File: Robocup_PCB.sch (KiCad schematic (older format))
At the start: 39 parts

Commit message: Finished schematic, started PCB Design
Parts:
- added D1: 1N5347B, Diode_THT:D_DO-201_P15.24mm_Horizontal, symbol Diode:1N53xxB
- added D2: GREEN, LED_SMD:LED_0805_2012Metric_Pad1.15x1.40mm_HandSolder, symbol Device:LED
- added J1: M1_ENOUT, Connector_PinSocket_2.54mm:PinSocket_1x02_P2.54mm_Vertical, symbol Connector:Conn_01x02_Male
- added J3: M2_ENOUT, Connector_PinSocket_2.54mm:PinSocket_1x02_P2.54mm_Vertical, symbol Connector:Conn_01x02_Male
- added J5: M3_ENOUT, Connector_PinSocket_2.54mm:PinSocket_1x02_P2.54mm_Vertical, symbol Connector:Conn_01x02_Male
- added J7: Arduino_Mega_Header, w_conn_misc:arduino_mega_header, symbol w_connectors:Arduino_Mega_Header
- added J8: XT60-M, 3rd party libs:AMASS_XT60-M, symbol XT60-M:XT60-M
- added Q1: IRF9540N, Package_TO_SOT_THT:TO-220-3_Vertical, symbol Transistor_FET:IRF9540N
- added Q2: IRFR120ZTRPBF, 3rd party libs:DPAK229P990X239-3N, symbol IRFR120ZTRPBF:IRFR120ZTRPBF
- added R13: 100k, Resistor_SMD:R_1206_3216Metric_Pad1.42x1.75mm_HandSolder, symbol Device:R
- added R14: 140R, Resistor_SMD:R_1206_3216Metric_Pad1.42x1.75mm_HandSolder, symbol Device:R
- added SW1: SS ESP101, Connector_PinSocket_2.54mm:PinSocket_1x03_P2.54mm_Vertical, symbol Switch:SW_SPDT
- added U1, U2: TB6612FNG_MOD, Robocup_PCB:U_TB6612FNG_MOD, symbol Robocup_PCB:TB6612FNG_MOD
- added U3: 5V_D24V5F5, Robocup_PCB:5V_D24V5F5_FP, symbol Robocup_PCB:5V_D24V5F5
- added U4: 12V_S18V20F12, Robocup_PCB:12_S18V20F12_FP, symbol Robocup_PCB:12V_S18V20F12
- C1, C10, C11, C12, C2, C3, C4, C5, C6, C7, C8, C9: value 1uF -> 0.1uF
- J2, J4, J6: renamed from J?; footprint (none) -> Connector_PinSocket_2.54mm:PinSocket_1x06_P2.54mm_Vertical
- R1, R10, R11, R12, R2, R3, R4, R5, R6, R7, R8, R9: value 62K -> 6k2
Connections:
- net labels added: +12V, +5V, M1_A, M1_AIN1, M1_AIN2, M1_B, M1_PWMA, M2_A, M2_B, M2_BIN1, M2_BIN2, M2_PWMB, M3_A, M3_AIN1, M3_AIN2, M3_B, M3_PWMA
- wire segments 72 -> 178
- no-connect marks 0 -> 69
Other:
- moved on the sheet: J2, J4, J6

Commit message: Redid power management, more efficient
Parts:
- removed Q2: IRFR120ZTRPBF, 3rd party libs:DPAK229P990X239-3N, symbol IRFR120ZTRPBF:IRFR120ZTRPBF
- added C?: 10n, symbol Device:C
- added D?: RED, LED_SMD:LED_0805_2012Metric_Pad1.15x1.40mm_HandSolder, symbol Device:LED
- added D?: BLUE, LED_SMD:LED_0805_2012Metric_Pad1.15x1.40mm_HandSolder, symbol Device:LED
- added R?: 680R, Resistor_SMD:R_1206_3216Metric_Pad1.42x1.75mm_HandSolder, symbol Device:R
- added R?: 180R, Resistor_SMD:R_1206_3216Metric_Pad1.42x1.75mm_HandSolder, symbol Device:R
- added SW? (x2): SS ESP101, Connector_PinSocket_2.54mm:PinSocket_1x03_P2.54mm_Vertical, symbol Switch:SW_SPDT
- R14: value 140R -> 680R
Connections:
- wire segments 178 -> 195
- no-connect marks 69 -> 70
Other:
- moved on the sheet: D1, D2, J8, Q1, R13, R14, SW1, U3, U4

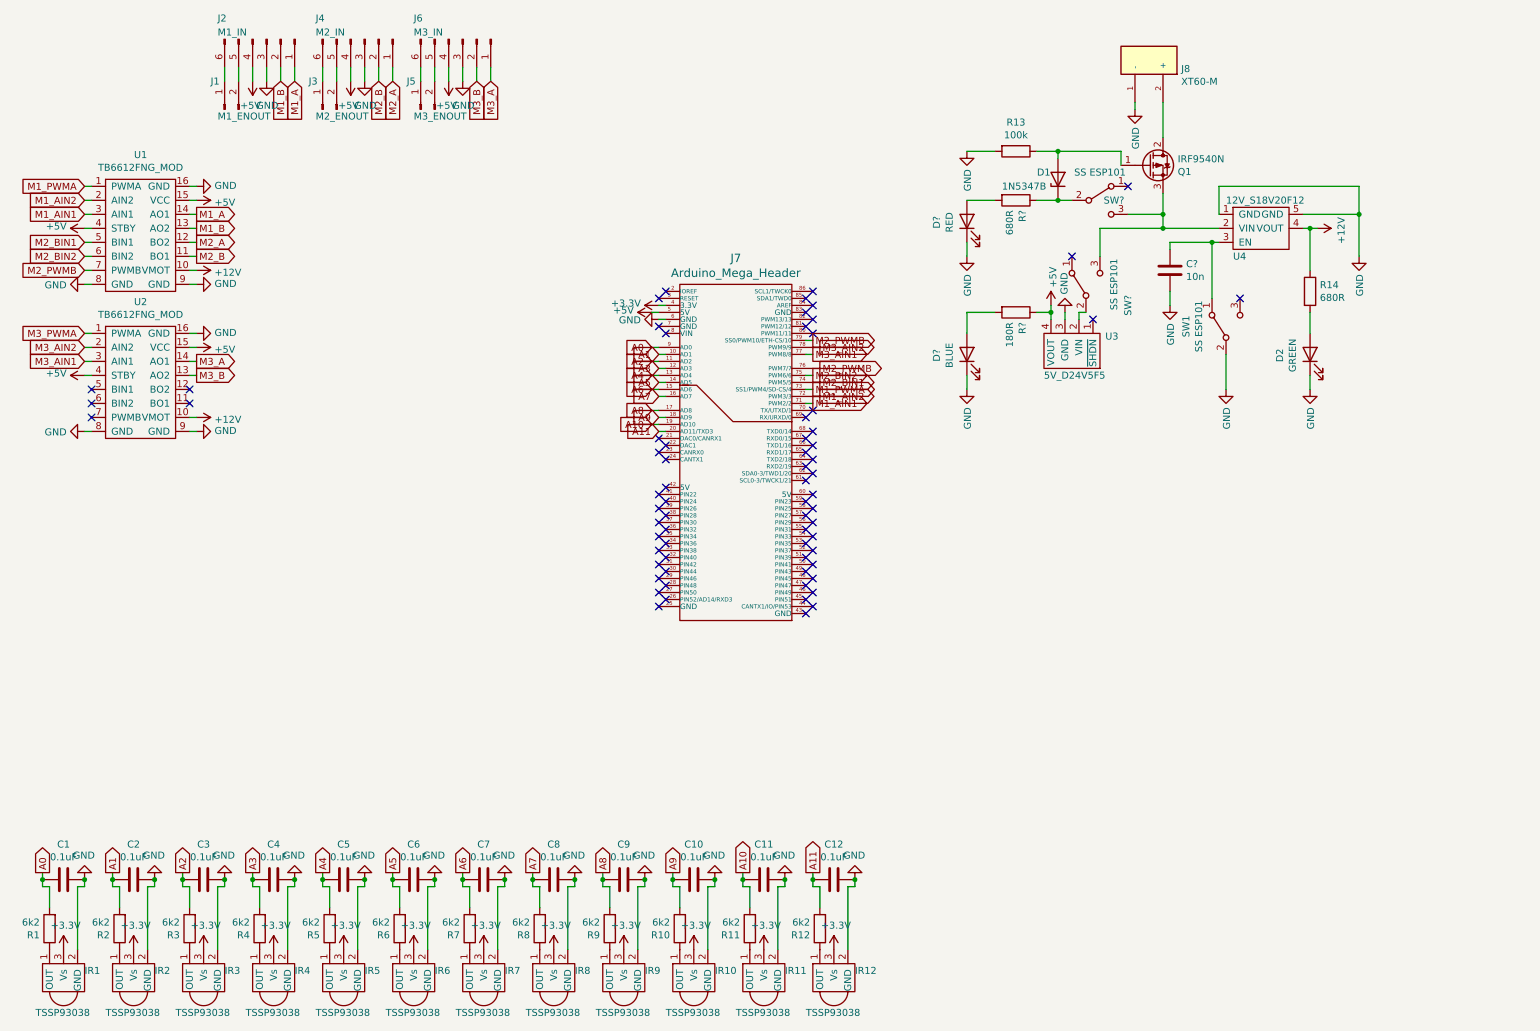
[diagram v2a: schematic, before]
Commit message: Parts given Footprints
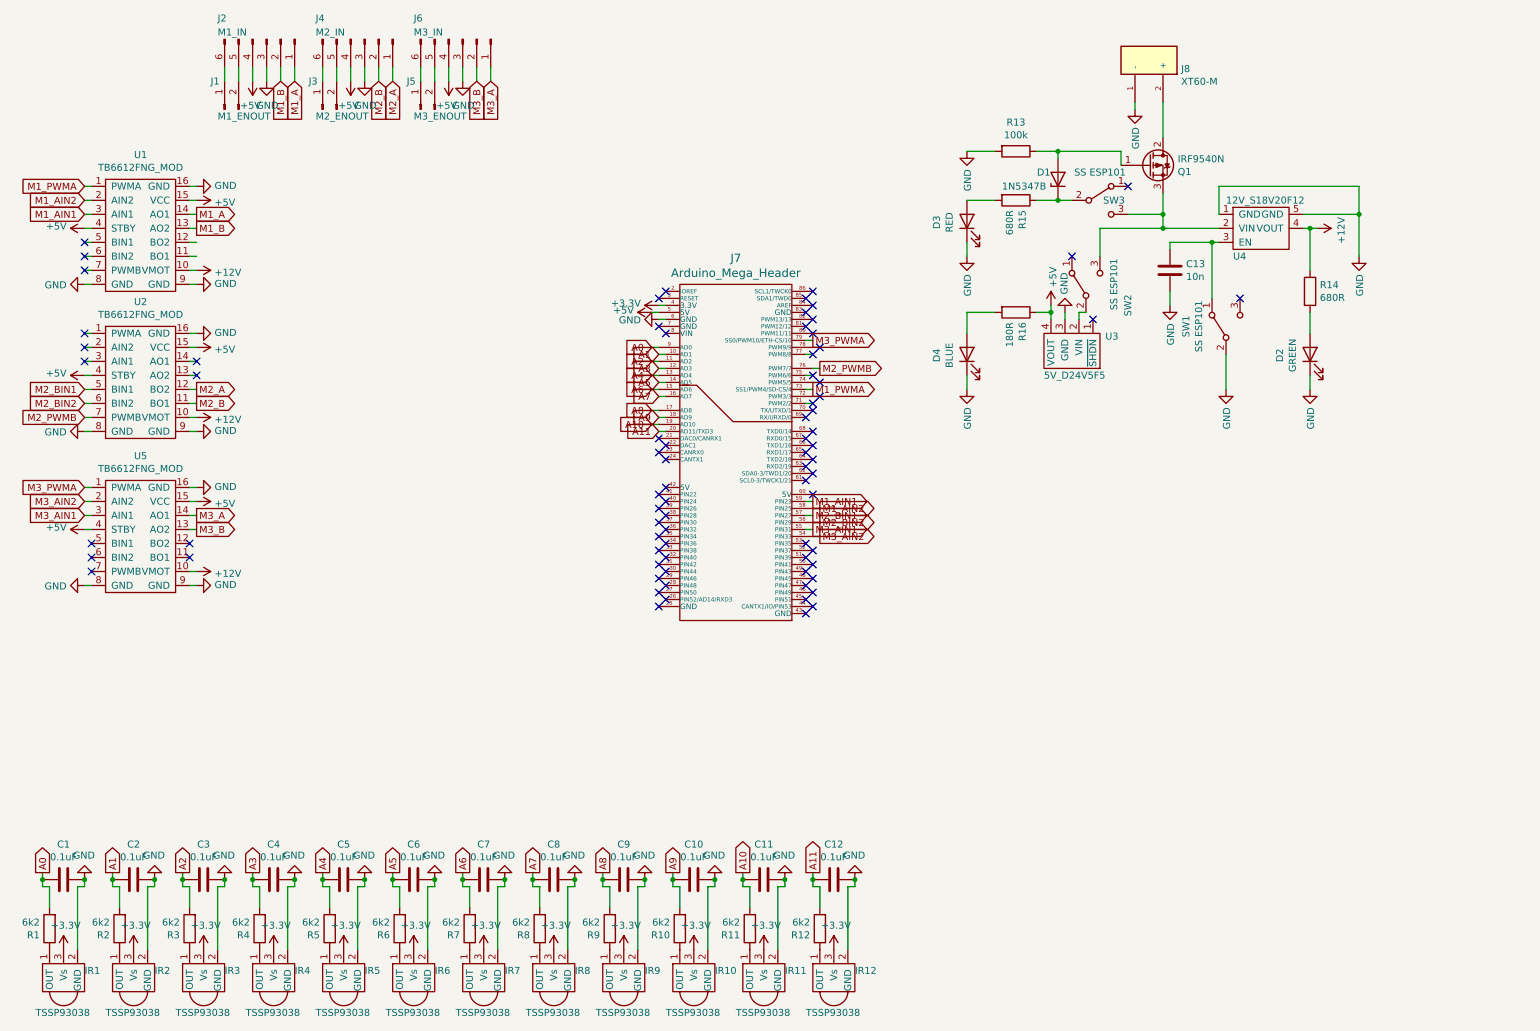
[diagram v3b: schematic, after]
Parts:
- added U2: TB6612FNG_MOD, Robocup_PCB:U_TB6612FNG_MOD, symbol Robocup_PCB:TB6612FNG_MOD
- C13: renamed from C?; footprint (none) -> Capacitor_SMD:C_0603_1608Metric_Pad1.05x0.95mm_HandSolder
- R13: footprint Resistor_SMD:R_1206_3216Metric_Pad1.42x1.75mm_HandSolder -> Resistor_SMD:R_0805_2012Metric_Pad1.15x1.40mm_HandSolder
- gave numbers to parts that had none: 6
- renumbered U2 to U5
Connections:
- net +12V: now also U2.10 (VMOT)
- net +5V: now also U2.15 (VCC), U2.4 (STBY)
- net GND: now also U2.16 (GND), U2.8 (GND), U2.9 (GND)
- net M1_AIN1: now also J7.59 (PIN23); no longer J7.71 (PWM2/2)
- net M1_AIN2: now also J7.58 (PIN25); no longer J7.72 (PWM3/3)
- net M2_A: now also U2.12 (BO2); no longer U1.12 (BO2)
- net M2_B: now also U2.11 (BO1); no longer U1.11 (BO1)
- net M2_BIN1: now also J7.57 (PIN27), U2.5 (BIN1); no longer J7.74 (PWM5/5), U1.5 (BIN1)
- net M2_BIN2: now also J7.56 (PIN29), U2.6 (BIN2); no longer J7.75 (PWM6/6), U1.6 (BIN2)
- net M2_PWMB: now also U2.7 (PWMB); no longer J7.79 (SS0/PWM10/ETH-CS/10), U1.7 (PWMB)
- net M3_AIN1: now also J7.55 (PIN31); no longer J7.77 (PWM8/8)
- net M3_AIN2: now also J7.54 (PIN33); no longer J7.78 (PWM9/9)
- net M3_PWMA: now also J7.79 (SS0/PWM10/ETH-CS/10)
- no-connect marks 70 -> 78
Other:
- moved on the sheet: U5

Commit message: Finished PCB, Generated Gerbers
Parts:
- removed J1: M1_ENOUT, Connector_PinSocket_2.54mm:PinSocket_1x02_P2.54mm_Vertical, symbol Connector:Conn_01x02_Male
- removed J3: M2_ENOUT, Connector_PinSocket_2.54mm:PinSocket_1x02_P2.54mm_Vertical, symbol Connector:Conn_01x02_Male
- removed J5: M3_ENOUT, Connector_PinSocket_2.54mm:PinSocket_1x02_P2.54mm_Vertical, symbol Connector:Conn_01x02_Male
- C13: footprint Capacitor_SMD:C_0603_1608Metric_Pad1.05x0.95mm_HandSolder -> Capacitor_SMD:C_1206_3216Metric_Pad1.42x1.75mm_HandSolder
- Q1: footprint Package_TO_SOT_THT:TO-220-3_Vertical -> Package_TO_SOT_SMD:TO-263-2
- R13: footprint Resistor_SMD:R_0805_2012Metric_Pad1.15x1.40mm_HandSolder -> Resistor_SMD:R_1206_3216Metric_Pad1.42x1.75mm_HandSolder
- U3: footprint Robocup_PCB:5V_D24V5F5_FP -> (none)
- renumbered J2 to J1, J4 to J2, J6 to J3, J7 to J4
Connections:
- net M3_ENB: now reaches J4.39 (PIN26)
- net M3_ENB: now also J3.6 (Pin_6)
- net M2_ENB: now reaches J4.40 (PIN24)
- net M2_ENB: now also J2.6 (Pin_6)
- net M1_ENB: now reaches J4.41 (PIN22)
- net M1_ENB: now also J1.6 (Pin_6)
- net M3_ENA: now reaches J4.62 (SDA0-3/TWD1/20)
- net M3_ENA: now also J3.5 (Pin_5)
- net M2_ENA: now reaches J4.63 (RXD2/19)
- net M2_ENA: now also J2.5 (Pin_5)
- net M1_ENA: now reaches J4.64 (TXD2/18)
- net M1_ENA: now also J1.5 (Pin_5)
- no-connect marks 78 -> 72
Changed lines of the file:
@@
 A11
 $Comp
-L Connector:Conn_01x06_Male J2
+L Connector:Conn_01x06_Male J1
 U 1 1 5FFBF4FE
 P 2250 750
-F 0 "J2" V 2100 400 50  0000 L CNN
+F 0 "J1" V 2100 400 50  0000 L CNN
 F 1 "M1_IN" V 2200 400 50  0000 L CNN
 F 2 "Connector_PinSocket_2.54mm:PinSocket_1x06_P2.54mm_Vertical" H 2250 750 50  0001 C CNN
@@
 $EndComp
 $Comp
-L Connector:Conn_01x06_Male J6
+L Connector:Conn_01x06_Male J3
 U 1 1 5FFC7622
 P 3650 750
-F 0 "J6" V 3500 400 50  0000 L CNN
+F 0 "J3" V 3500 400 50  0000 L CNN
 F 1 "M3_IN" V 3600 400 50  0000 L CNN
 F 2 "Connector_PinSocket_2.54mm:PinSocket_1x06_P2.54mm_Vertical" H 3650 750 50  0001 C CNN
@@
 $EndComp
 $Comp
-L Connector:Conn_01x06_Male J4
+L Connector:Conn_01x06_Male J2
 U 1 1 5FFC2FEB
 P 2950 750
-F 0 "J4" V 2800 400 50  0000 L CNN
+F 0 "J2" V 2800 400 50  0000 L CNN
 F 1 "M2_IN" V 2900 400 50  0000 L CNN
 F 2 "Connector_PinSocket_2.54mm:PinSocket_1x06_P2.54mm_Vertical" H 2950 750 50  0001 C CNN
@@
 $EndComp
 $Comp
-L w_connectors:Arduino_Mega_Header J7
+L w_connectors:Arduino_Mega_Header J4
 U 1 1 5FF3CCD5
 P 5600 3700
-F 0 "J7" H 5600 5087 60  0000 C CNN
+F 0 "J4" H 5600 5087 60  0000 C CNN
 F 1 "Arduino_Mega_Header" H 5600 4981 60  0000 C CNN
 F 2 "w_conn_misc:arduino_mega_header" H 5600 3700 60  0001 C CNN
@@
 Wire Wire Line
 	2150 950  2150 1050
-$Comp
-L Connector:Conn_01x02_Male J5
-U 1 1 6006A0CE
-P 3350 1250
-F 0 "J5" V 3550 1350 50  0000 R CNN
-F 1 "M3_ENOUT" V 3300 1300 50  0000 R CNN
-F 2 "Connector_PinSocket_2.54mm:PinSocket_1x02_P2.54mm_Vertical" H 3350 1250 50  0001 C CNN
-F 3 "~" H 3350 1250 50  0001 C CNN
-	1    3350 1250
-	0    -1   -1   0
-$EndComp
-$Comp
-L Connector:Conn_01x02_Male J3
-U 1 1 6006B547
-P 2650 1250
-F 0 "J3" V 2850 1350 50  0000 R CNN
-F 1 "M2_ENOUT" V 2600 1300 50  0000 R CNN
-F 2 "Connector_PinSocket_2.54mm:PinSocket_1x02_P2.54mm_Vertical" H 2650 1250 50  0001 C CNN
-F 3 "~" H 2650 1250 50  0001 C CNN
-	1    2650 1250
-	0    -1   -1   0
-$EndComp
-$Comp
-L Connector:Conn_01x02_Male J1
-U 1 1 6006BCDF
-P 1950 1250
-F 0 "J1" V 2150 1350 50  0000 R CNN
-F 1 "M1_ENOUT" V 1900 1300 50  0000 R CNN
-F 2 "Connector_PinSocket_2.54mm:PinSocket_1x02_P2.54mm_Vertical" H 1950 1250 50  0001 C CNN
-F 3 "~" H 1950 1250 50  0001 C CNN
-	1    1950 1250
-	0    -1   -1   0
-$EndComp
-Wire Wire Line
-	3450 950  3450 1050
-Wire Wire Line
-	3350 950  3350 1050
-Wire Wire Line
-	2750 950  2750 1050
-Wire Wire Line
-	2650 950  2650 1050
-Wire Wire Line
-	2050 950  2050 1050
-Wire Wire Line
-	1950 950  1950 1050
 Text GLabel 1750 2000 2    50   Output ~ 0
 M1_A
@@
 NoConn ~ 6150 3650
 NoConn ~ 6100 3700
-NoConn ~ 6150 3750
-NoConn ~ 6100 3800
-NoConn ~ 6150 3850
 NoConn ~ 6100 3900
 NoConn ~ 6150 4000
@@
 NoConn ~ 5050 4200
 NoConn ~ 5100 4150
-NoConn ~ 5050 4100
-NoConn ~ 5100 4050
-NoConn ~ 5050 4000
 NoConn ~ 5100 3950
 $Comp
@@
 F 0 "Q1" H 8755 1604 50  0000 L CNN
 F 1 "IRF9540N" H 8755 1695 50  0000 L CNN
-F 2 "Package_TO_SOT_THT:TO-220-3_Vertical" H 8750 1575 50  0001 L CIN
+F 2 "Package_TO_SOT_SMD:TO-263-2" H 8750 1575 50  0001 L CIN
 F 3 "http://www.irf.com/product-info/datasheets/data/irf9540n.pdf" H 8550 1650 50  0001 L CNN
 	1    8550 1650
@@
 F 0 "R13" V 7393 1550 50  0000 C CNN
 F 1 "100k" V 7484 1550 50  0000 C CNN
-F 2 "Resistor_SMD:R_0805_2012Metric_Pad1.15x1.40mm_HandSolder" V 7530 1550 50  0001 C CNN
+F 2 "Resistor_SMD:R_1206_3216Metric_Pad1.42x1.75mm_HandSolder" V 7530 1550 50  0001 C CNN
 F 3 "~" H 7600 1550 50  0001 C CNN
 	1    7600 1550
@@
 Wire Wire Line
 	9750 2100 9700 2100
-$Comp
-L Robocup_PCB:5V_D24V5F5 U3
-U 1 1 604D36B7
-P 8000 2950
-F 0 "U3" H 7762 2871 50  0000 R CNN
-F 1 "5V_D24V5F5" H 8200 3150 50  0000 R CNN
-F 2 "Robocup_PCB:5V_D24V5F5_FP" H 7950 2900 50  0001 C CNN
-F 3 "" H 7950 2900 50  0001 C CNN
-	1    8000 2950
-	-1   0    0    1
-$EndComp
 NoConn ~ 8150 2750
 $Comp
@@
 F 0 "C13" H 8815 2446 50  0000 L CNN
 F 1 "10n" H 8815 2355 50  0000 L CNN
-F 2 "Capacitor_SMD:C_0603_1608Metric_Pad1.05x0.95mm_HandSolder" H 8738 2250 50  0001 C CNN
+F 2 "Capacitor_SMD:C_1206_3216Metric_Pad1.42x1.75mm_HandSolder" H 8738 2250 50  0001 C CNN
 F 3 "~" H 8700 2400 50  0001 C CNN
 	1    8700 2400
@@
 	-1   0    0    1
 $EndComp
+Text GLabel 2050 1100 3    50   Output ~ 0
+M1_ENA
+Wire Wire Line
+	2050 950  2050 1100
+Text GLabel 6200 3750 2    50   Input ~ 0
+M1_ENA
+Wire Wire Line
+	6150 3750 6200 3750
+Text GLabel 2750 1100 3    50   Output ~ 0
+M2_ENA
+Wire Wire Line
+	2750 950  2750 1100
+Text GLabel 3450 1100 3    50   Output ~ 0
+M3_ENA
+Wire Wire Line
+	3450 950  3450 1100
+Text GLabel 6150 3800 2    50   Input ~ 0
+M2_ENA
+Wire Wire Line
+	6100 3800 6150 3800
+Text GLabel 6200 3850 2    50   Input ~ 0
+M3_ENA
+Wire Wire Line
+	6150 3850 6200 3850
+Text GLabel 1950 1100 3    50   Output ~ 0
+M1_ENB
+Wire Wire Line
+	1950 950  1950 1100
+Text GLabel 5000 4000 0    50   Input ~ 0
+M1_ENB
+Wire Wire Line
+	5000 4000 5050 4000
+Text GLabel 2650 1100 3    50   Output ~ 0
+M2_ENB
+Wire Wire Line
+	2650 950  2650 1100
+Text GLabel 3350 1100 3    50   Output ~ 0
+M3_ENB
+Wire Wire Line
+	3350 950  3350 1100
+Text GLabel 5050 4050 0    50   Input ~ 0
+M2_ENB
+Wire Wire Line
+	5050 4050 5100 4050
+Text GLabel 5000 4100 0    50   Input ~ 0
+M3_ENB
+Wire Wire Line
+	5000 4100 5050 4100
+$Comp
+L Robocup_PCB:5V_D24V5F5 U3
+U 1 1 6007652D
+P 8000 2950
+F 0 "U3" H 7762 2871 50  0000 R CNN
+F 1 "5V_D24V5F5" H 7762 2962 50  0000 R CNN
+F 2 "" H 7950 2900 50  0001 C CNN
+F 3 "" H 7950 2900 50  0001 C CNN
+	1    8000 2950
+	-1   0    0    1
+$EndComp
